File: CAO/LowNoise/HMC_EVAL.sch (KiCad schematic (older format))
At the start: 57 parts, among them J1 Conn_01x03, J2 Conn_01x03, Q1 IRF7319IPBF, SW1 SW_Push, U1 OPA2209, U2 HMC1001, U4 INA128

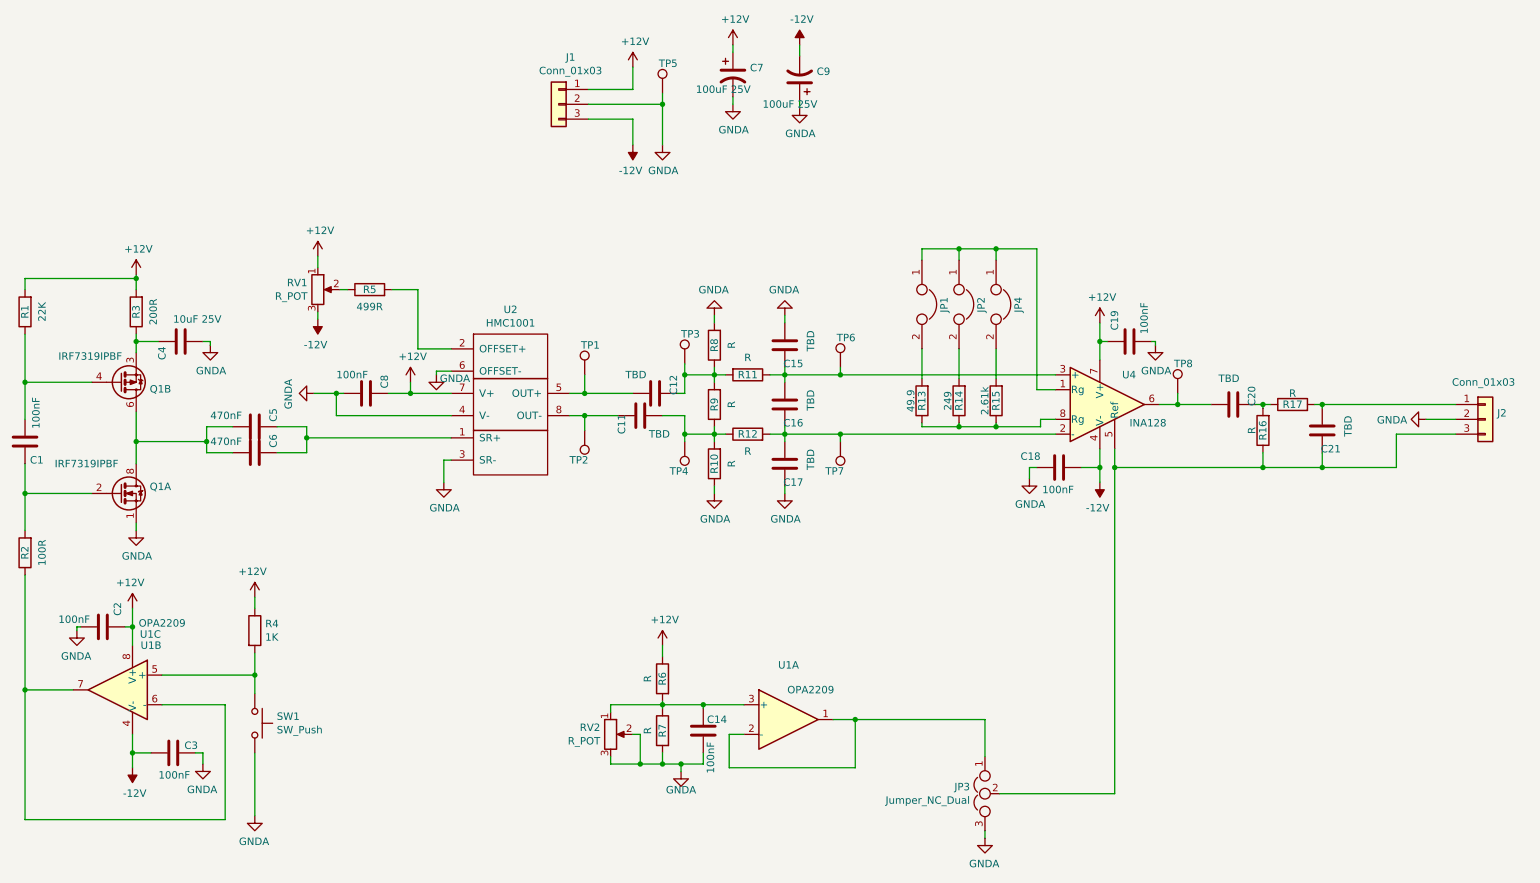
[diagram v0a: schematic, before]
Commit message: - Low noise version is finish. - Add serigraphi on two design. - Qestion: Copper plane will block low freqency(200hz) magnetic wave??
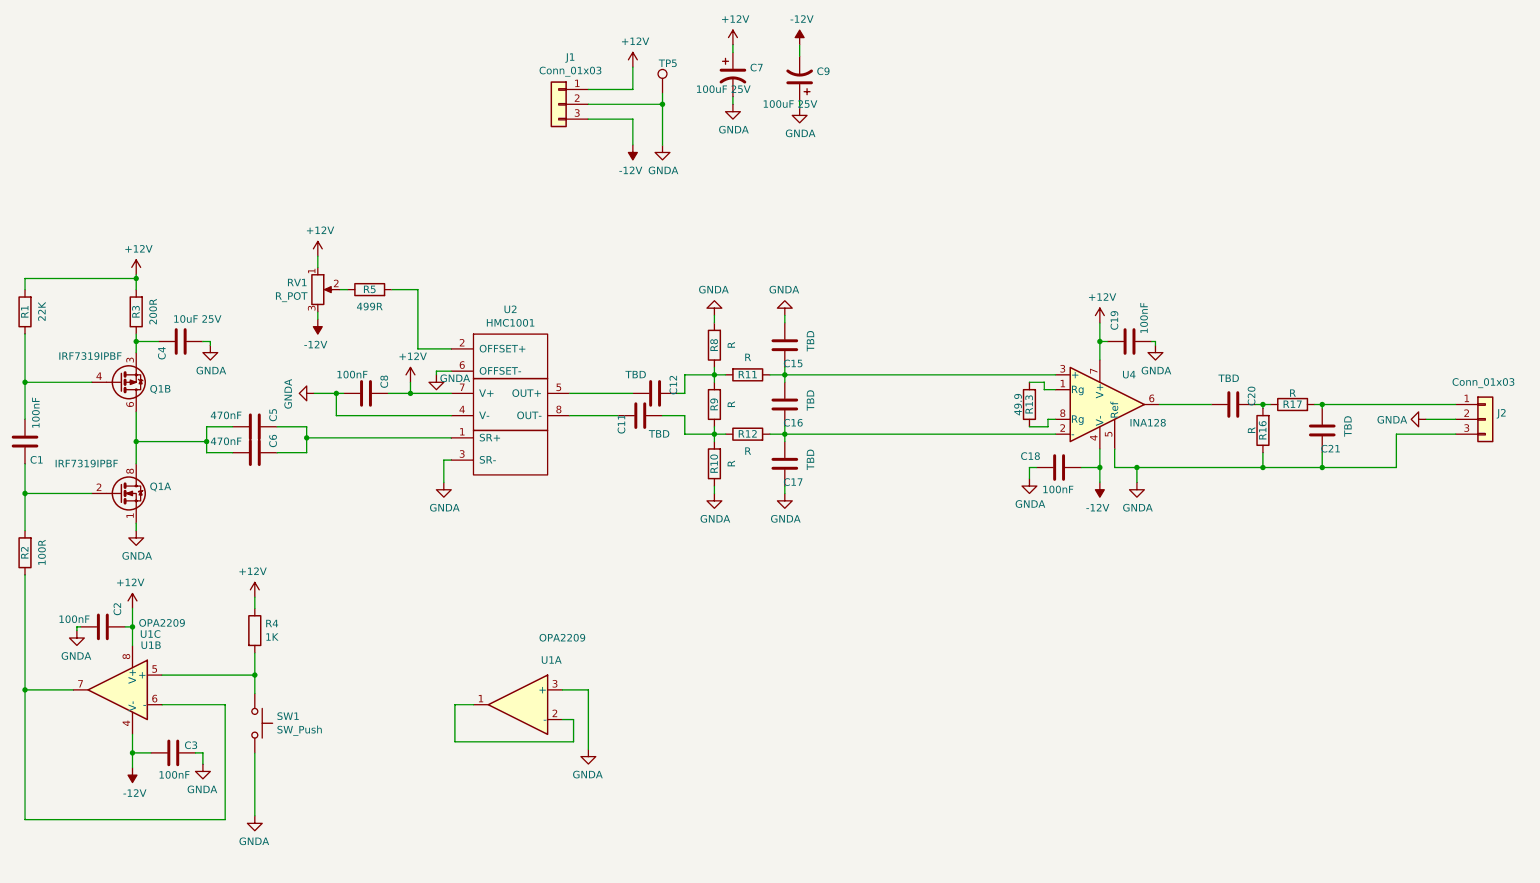
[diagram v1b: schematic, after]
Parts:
- removed C14: 100nF, Capacitors_SMD:C_0805_HandSoldering, symbol Device:C
- removed JP1, JP2, JP4: Jumper, Connectors_Samtec:SL-102-X-XX_1x02, symbol Device:Jumper
- removed JP3: Jumper_NC_Dual, Connectors_Samtec:SL-103-X-XX_1x03, symbol Device:Jumper_NC_Dual
- removed R14: 249, Resistors_SMD:R_0805_HandSoldering, symbol Device:R
- removed R15: 2.61k, Resistors_SMD:R_0805_HandSoldering, symbol Device:R
- removed R6, R7: R, Resistors_SMD:R_0805_HandSoldering, symbol Device:R
- removed RV2: R_POT, Potentiometers:Potentiometer_Trimmer_Bourns_3296W, symbol Device:R_POT
- removed TP1, TP2, TP3, TP4, TP6, TP7, TP8: TestPoint, Connectors_Samtec:SL-101-X-XX_1x01, symbol Connector:TestPoint
- U1: supplier Farnell: 1862577 -> (none)
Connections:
- net GNDA: now also C21.1, J2.3 (Pin_3), R16.1, U1.3 (+), U4.5 (Ref)
- net at U4.1 (Rg): now also R13.2
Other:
- moved on the sheet: R13
